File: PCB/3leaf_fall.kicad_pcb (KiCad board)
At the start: 2 copper layers, 146.7 x 75.4 mm, 62 parts, among them J1 5034801600, J2 USB_C_Receptacle_USB2.0_16P, SW1 Switch, U1 HOLYIOT-18010-NRF52840, U3 BQ24075RGT, U4 XC6220B331MR

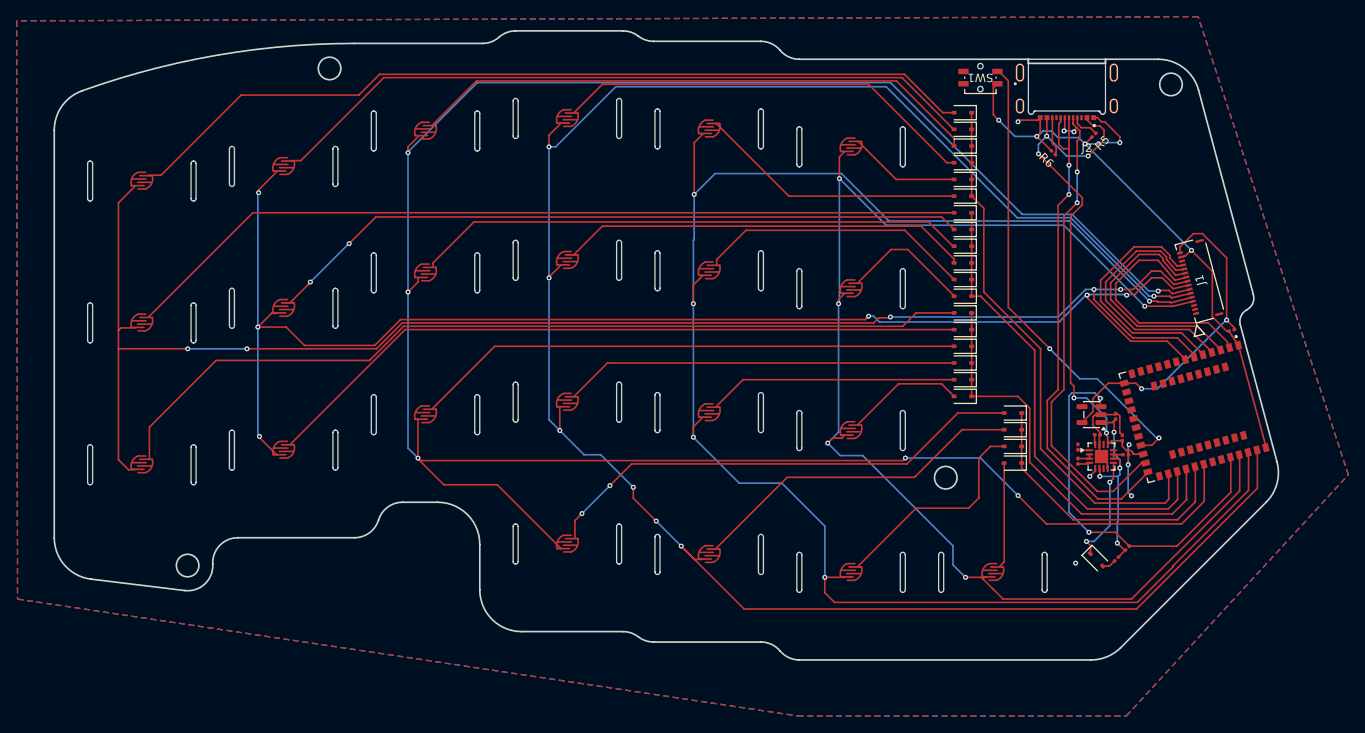
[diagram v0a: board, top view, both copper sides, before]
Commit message: Near completion
* Updated switch footprint to meet PCB fab reqs
* Chose Raytac MDBT42 MCU
* Removed diodes
* Updated traces for diodeless config
* Added CR2032 battery contacts
* Removed USB board cutout

* More planning for battery mount
* Magnetic reed switch for power on/off
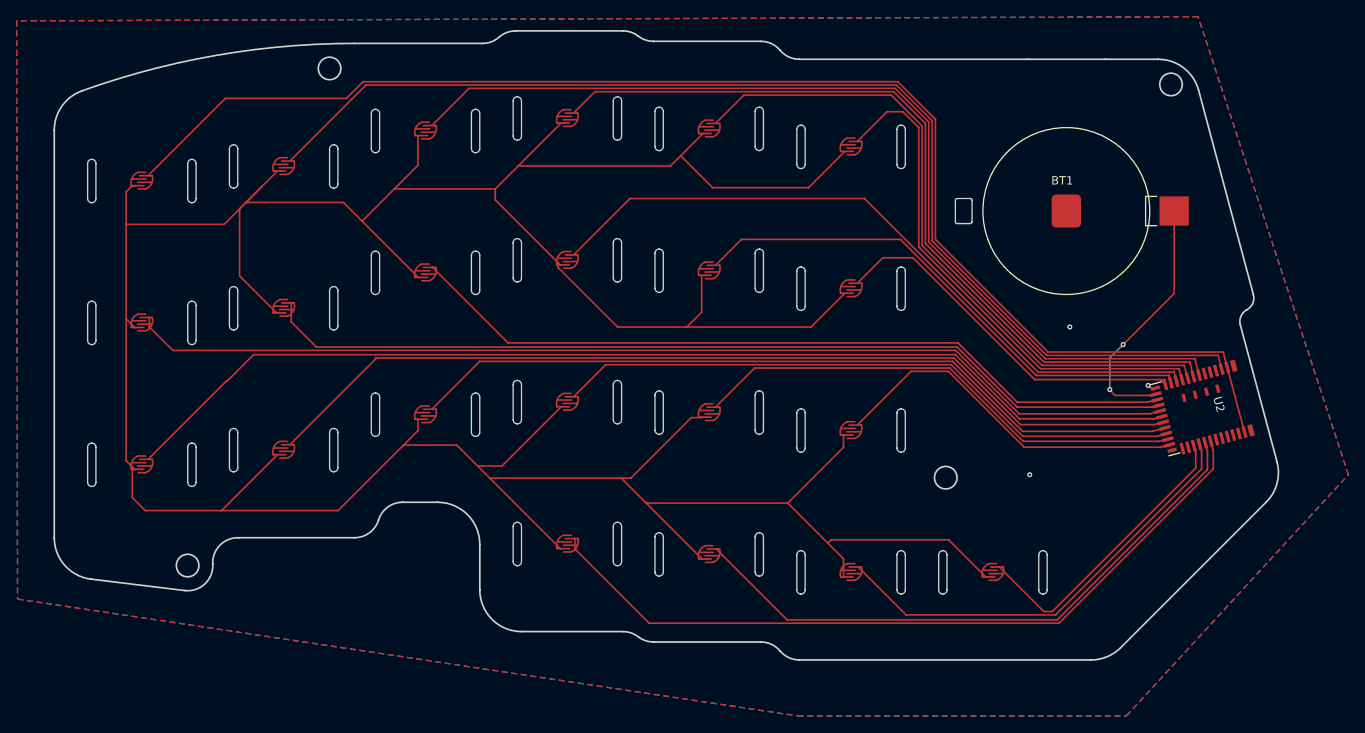
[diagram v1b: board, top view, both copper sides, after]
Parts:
- removed C1, C2, C3, C4, C5: C, keeblib:C_0201_0603Metric
- removed D1, D10, D11, D12, D13, D14, D15, D16, D17, D18, D19, D2, D20, D21, D22, D3, D4, D5, D6, D7, D8, D9: Diode, Diode_SMD:D_SOD-323
- removed D23: 1N4148W, Diode_SMD:D_SOD-323
- removed J1: 5034801600, keeblib:CON_5034801600_MOL
- removed J2: USB_C_Receptacle_USB2.0_16P, keeblib:GCT_USB4500-03-1-A_REVA
- removed R1, R2, R3: 10k, keeblib:R_0201_0603Metric
- removed R4: 10m, keeblib:R_0201_0603Metric
- removed R5: 5.1k, keeblib:R_0201_0603Metric
- removed R6: 5.1, keeblib:R_0201_0603Metric
- removed SW1: Switch, keeblib:EVQ_P7_PUC
- removed U1: HOLYIOT-18010-NRF52840, keeblib:XCVR_HOLYIOT-18010-NRF52840
- removed U3: BQ24075RGT, Package_DFN_QFN:VQFN-16-1EP_3x3mm_P0.5mm_EP1.6x1.6mm
- removed U4: XC6220B331MR, Package_TO_SOT_SMD:SOT-23-5
- added BT1: 110, keeblib:BAT_110_2032, F.Cu at (219.2, 62.3)
- added U2: ~, keeblib:Raytac_MDBT42, F.Cu at (237.0, 85.6)
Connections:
- S1 pad 1: Col0 -> GND
- S1 pad 2: Net-(D1-A) -> S1
- S10 pad 1: Col3 -> GND
- S10 pad 2: Net-(D10-A) -> S10
- S11 pad 1: Col4 -> GND
- S11 pad 2: Net-(D11-A) -> S11
- S12 pad 1: Col5 -> GND
- S12 pad 2: Net-(D12-A) -> S12
- S13 pad 1: Col0 -> GND
- S13 pad 2: Net-(D13-A) -> S13
- S14 pad 1: Col1 -> GND
- S14 pad 2: Net-(D14-A) -> S14
- S15 pad 1: Col2 -> GND
- S15 pad 2: Net-(D15-A) -> S15
- S16 pad 1: Col3 -> GND
- S16 pad 2: Net-(D16-A) -> S16
- S17 pad 1: Col4 -> GND
- S17 pad 2: Net-(D17-A) -> S17
- S18 pad 1: Col5 -> GND
- S18 pad 2: Net-(D18-A) -> S18
- S19 pad 1: Col0 -> GND
- S19 pad 2: Net-(D19-A) -> S19
- S2 pad 1: Col1 -> GND
- S2 pad 2: Net-(D2-A) -> S2
- S20 pad 1: Col1 -> GND
- S20 pad 2: Net-(D20-A) -> S20
- S21 pad 1: Col2 -> GND
- S21 pad 2: Net-(D21-A) -> S21
- S22 pad 1: Col3 -> GND
- S22 pad 2: Net-(D22-A) -> S22
- S3 pad 1: Col2 -> GND
- S3 pad 2: Net-(D3-A) -> S3
- S4 pad 1: Col3 -> GND
- S4 pad 2: Net-(D4-A) -> S4
- S5 pad 1: Col4 -> GND
- S5 pad 2: Net-(D5-A) -> S5
- S6 pad 1: Col5 -> GND
- S6 pad 2: Net-(D6-A) -> S6
- S7 pad 1: Col0 -> GND
- S7 pad 2: Net-(D7-A) -> S7
- S8 pad 1: Col1 -> GND
- S8 pad 2: Net-(D8-A) -> S8
- S9 pad 1: Col2 -> GND
- S9 pad 2: Net-(D9-A) -> S9
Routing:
- net GND: track 103.9 -> 435.8 mm, vias 11 -> 3
- net Col3: track 279.3 -> 0.00 mm, vias 6 -> 0
- net Col2: track 240.2 -> 0.00 mm, vias 7 -> 0
- net Col1: track 202.6 -> 0.00 mm, vias 5 -> 0
- net Col5: track 187.2 -> 0.00 mm, vias 5 -> 0
- net Col4: track 171.1 -> 0.00 mm, vias 6 -> 0
- net S6: track 0.00 -> 165.2 mm
- net Col0: track 157.3 -> 0.00 mm, vias 5 -> 0
- net S5: track 0.00 -> 138.5 mm
- net S18: track 0.00 -> 129.8 mm
- net S12: track 0.00 -> 126.8 mm
- net S4: track 0.00 -> 117.1 mm
- net S17: track 0.00 -> 112.3 mm
- net S11: track 0.00 -> 110.6 mm
- net Net-(D18-A): track 105.9 -> 0.00 mm
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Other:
- outline, holes or cut-outs redrawn

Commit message: Add initial firmware, dongle
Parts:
- removed U2: ~, keeblib:Raytac_MDBT42
- added U1: ~, keeblib:Raytac_MDBT42Q_P, F.Cu at (234.5, 86.3)
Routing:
- net S6: track 165.2 -> 153.3 mm
- net S22: track 92.5 -> 87.7 mm
- net S21: track 73.2 -> 68.4 mm
- net S20: track 53.9 -> 49.3 mm
- net S19: track 35.6 -> 31.2 mm
- net S7: track 44.4 -> 40.1 mm
- net S5: track 138.5 -> 134.5 mm
- net S13: track 43.8 -> 40.5 mm
- net S14: track 59.8 -> 56.6 mm
- net S15: track 76.2 -> 73.1 mm
- net S16: track 93.7 -> 90.8 mm
- net VCC: track 30.5 -> 27.7 mm
- net S17: track 112.3 -> 109.7 mm
- net S4: track 117.1 -> 114.7 mm
- net S3: track 98.5 -> 96.1 mm
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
